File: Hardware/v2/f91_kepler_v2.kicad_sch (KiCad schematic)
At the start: 89 parts, among them J1 LS013B7DH03 FPC, Q1 FS8205A, SW1 BTN1/BSL, SW2 BTN2, SW3 BTN3, U1 CC2652R7RGZ, U2 BQ51050B, U3 DW01A, U4 XC6206P302MR, U5 LIS2DW12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

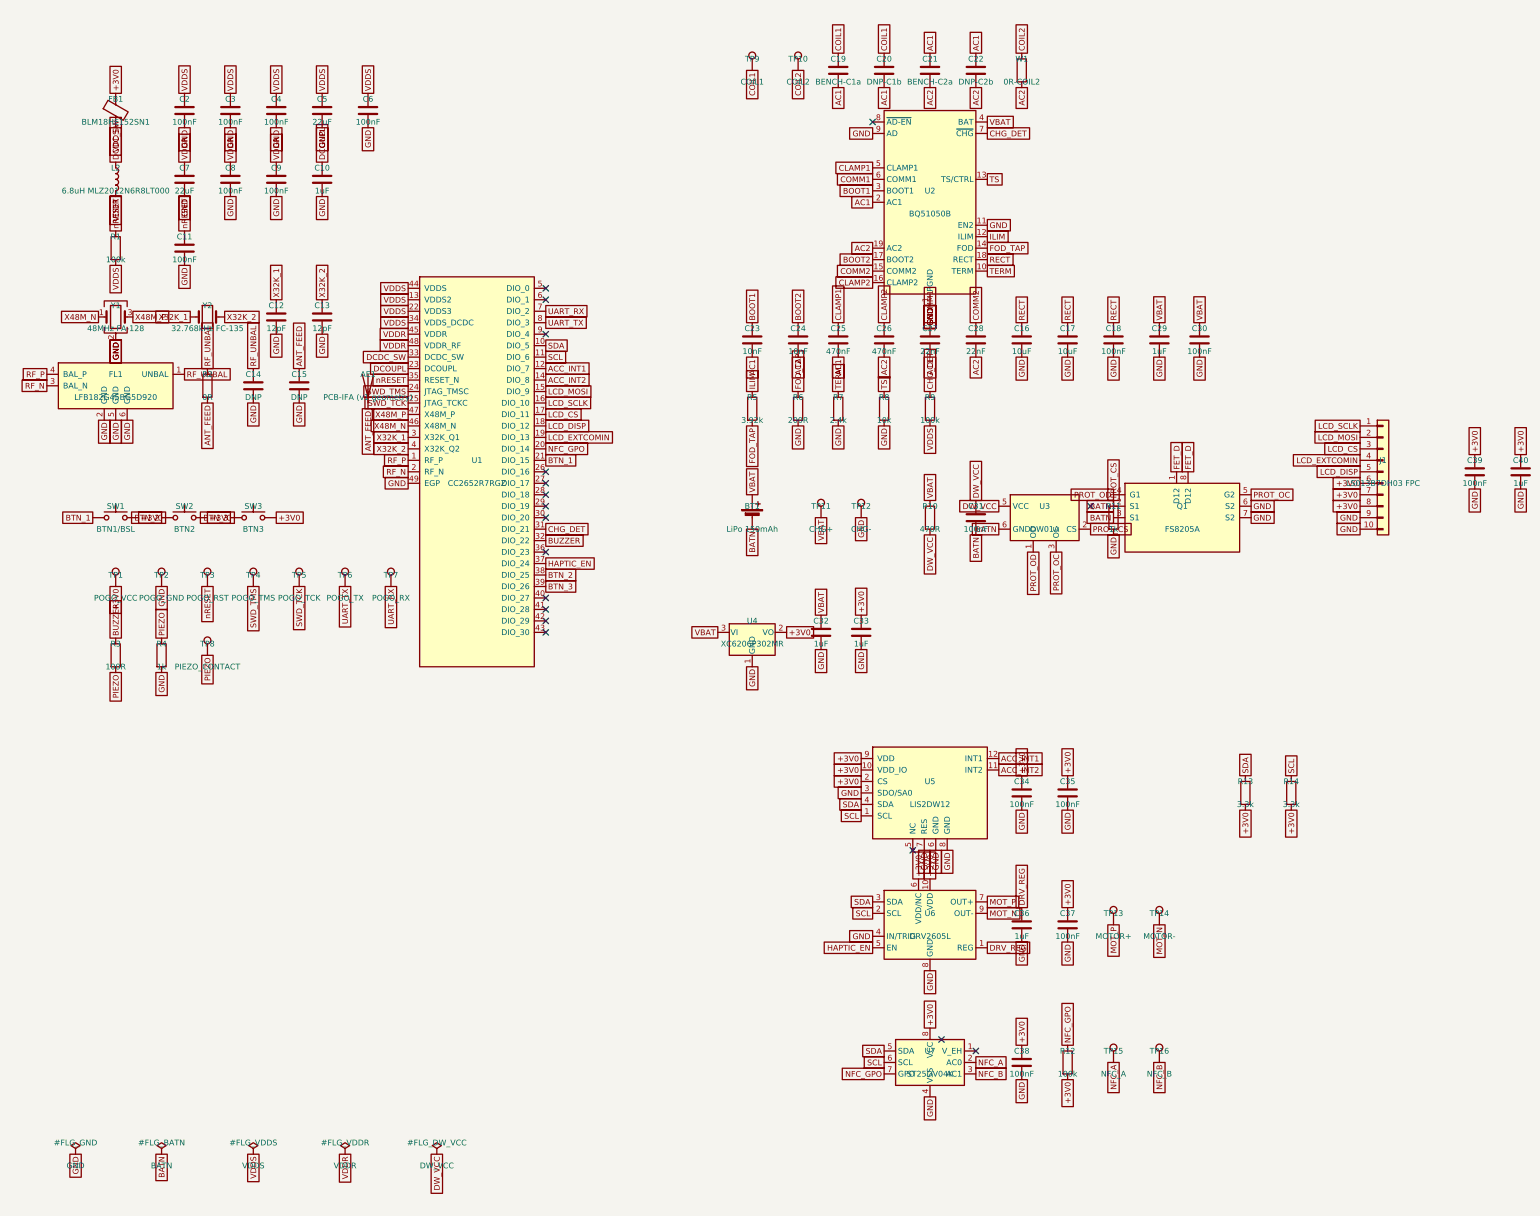
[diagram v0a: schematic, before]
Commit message: fix(hw/v2): sync AE1 schematic symbol to chip antenna
Update AE1 in the schematic to match the PCB chip-antenna swap:
- Value: "PCB-IFA (v1 geometry)" -> "2450AT18A100"
- Footprint: f91_footprints:ANT_v1_IFA -> f91_footprints:ANT_2450AT18A100

Device:Antenna symbol kept (pin1 = Feed = ANT_FEED, matches board pad1);
footprint pad2 (NC) is an unmapped mechanical pad, which KiCad allows.
schematic-parity: AE1 has no net conflict. The remaining parity items
(105 blank-lib-nickname footprint mismatches, 17 unconnected-GPIO net
entries, 1 stray pin) are pre-existing project-wide noise, not from this
change.
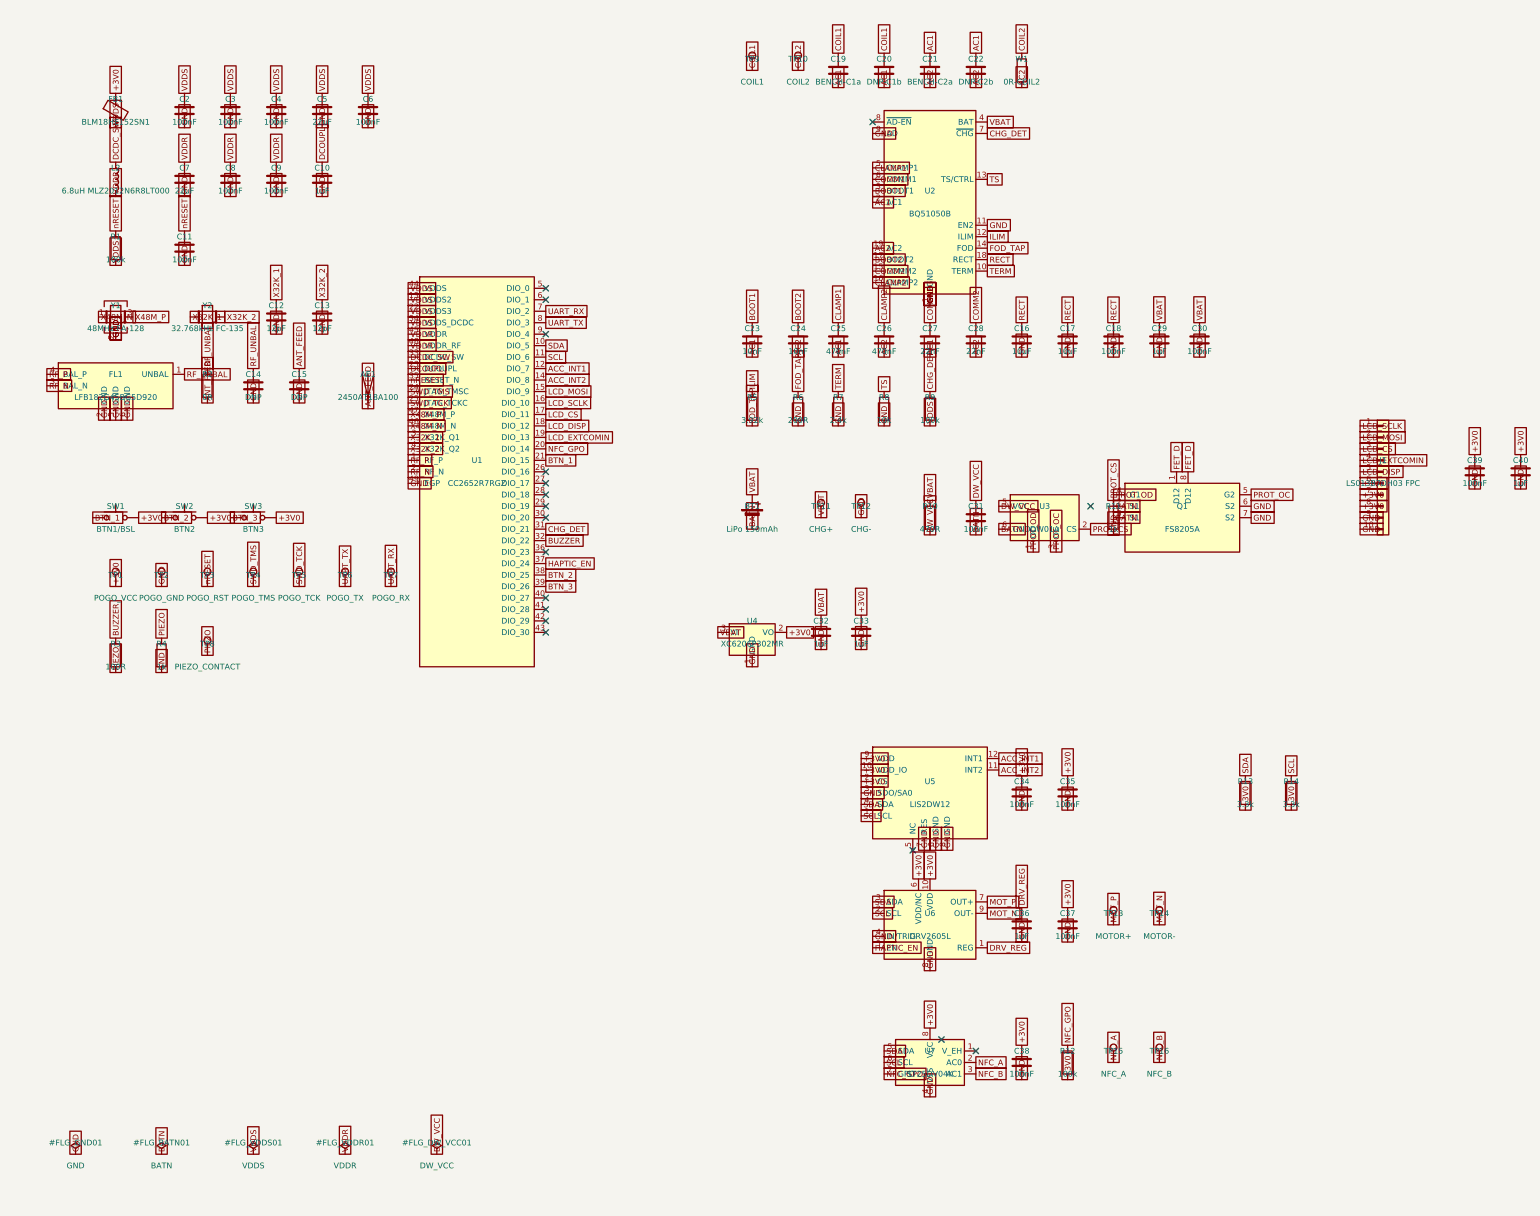
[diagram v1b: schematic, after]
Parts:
- AE1: value PCB-IFA (v1 geometry) -> 2450AT18A100; footprint f91_footprints:ANT_v1_IFA -> f91_footprints:ANT_2450AT18A100

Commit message: fix(hw/v2): close PCB<->schematic parity debt (123 -> 1)
Board was generated with blank footprint library nicknames and a few
metadata gaps, producing 123 schematic-parity mismatches that would fight
"update PCB from schematic". Closed almost all:

- fix_fpids.py: set each board footprint FPID nickname from the schematic
  (item names already matched -> no geometry change). Clears 105 name
  mismatches.
- fix_tp_bom.py: TP1-16 symbols in_bom/in_pos_files yes -> no. Test points
  (pogo pads + taps) are not orderable BOM parts; the footprints already
  excluded them. Clears 16 attribute mismatches.
- fix_unconnected_nets.py: assign the schematic's single-pad
  "unconnected-(...)" nets (spare U1/U2/U3/U5/U7 pins) to the matching
  netless board pads. Clears 17 net_conflicts.

Remaining (all benign, documented):
- parity 1: U7 ST25DV symbol pin 9 = "NC" (hidden); SO8 footprint correctly
  has no pad 9. KiCad flags NC pins without pads as warnings.
- ERC 2: U4 lib_symbol_mismatch (stale embedded copy vs Regulator_Linear;
  fix via Eeschema "Update Symbols from Library"); U5 pin_to_pin (SDO/SA0
  tied to GND for I2C address select — intentional, ERC false positive).

DRC fab-blocking still 0. Schematic migrated f91gen -> eeschema format.
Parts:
- TP1, TP10, TP11, TP12, TP13, TP14, TP15, TP16, TP2, TP3, TP4, TP5, TP6, TP7, TP8, TP9: now left out of the parts list
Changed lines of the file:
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@@
 		(body_style 1)
 		(exclude_from_sim no)
-		(in_bom yes)
+		(in_bom no)
 		(on_board yes)
-		(in_pos_files yes)
+		(in_pos_files no)
 		(dnp no)
 		(property "Reference" "TP3"
@@
 		(body_style 1)
 		(exclude_from_sim no)
-		(in_bom yes)
+		(in_bom no)
 		(on_board yes)
-		(in_pos_files yes)
+		(in_pos_files no)
 		(dnp no)
 		(property "Reference" "TP7"
@@
 		(body_style 1)
 		(exclude_from_sim no)
-		(in_bom yes)
+		(in_bom no)
 		(on_board yes)
-		(in_pos_files yes)
+		(in_pos_files no)
 		(dnp no)
 		(property "Reference" "TP13"
@@
 		(body_style 1)
 		(exclude_from_sim no)
-		(in_bom yes)
+		(in_bom no)
 		(on_board yes)
-		(in_pos_files yes)
+		(in_pos_files no)
 		(dnp no)
 		(property "Reference" "TP14"
@@
 		(body_style 1)
 		(exclude_from_sim no)
-		(in_bom yes)
+		(in_bom no)
 		(on_board yes)
-		(in_pos_files yes)
+		(in_pos_files no)
 		(dnp no)
 		(property "Reference" "TP10"
@@
 		(body_style 1)
 		(exclude_from_sim no)
-		(in_bom yes)
+		(in_bom no)
 		(on_board yes)
-		(in_pos_files yes)
+		(in_pos_files no)
 		(dnp no)
 		(property "Reference" "TP5"
@@
 		(body_style 1)
 		(exclude_from_sim no)
-		(in_bom yes)
+		(in_bom no)
 		(on_board yes)
-		(in_pos_files yes)
+		(in_pos_files no)
 		(dnp no)
 		(property "Reference" "TP1"
@@
 		(body_style 1)
 		(exclude_from_sim no)
-		(in_bom yes)
+		(in_bom no)
 		(on_board yes)
-		(in_pos_files yes)
+		(in_pos_files no)
 		(dnp no)
 		(property "Reference" "TP11"
@@
 		(body_style 1)
 		(exclude_from_sim no)
-		(in_bom yes)
+		(in_bom no)
 		(on_board yes)
-		(in_pos_files yes)
+		(in_pos_files no)
 		(dnp no)
 		(property "Reference" "TP9"
@@
 		(body_style 1)
 		(exclude_from_sim no)
-		(in_bom yes)
+		(in_bom no)
 		(on_board yes)
-		(in_pos_files yes)
+		(in_pos_files no)
 		(dnp no)
 		(property "Reference" "TP2"
@@
 		(body_style 1)
 		(exclude_from_sim no)
-		(in_bom yes)
+		(in_bom no)
 		(on_board yes)
-		(in_pos_files yes)
+		(in_pos_files no)
 		(dnp no)
 		(property "Reference" "TP16"
@@
 		(body_style 1)
 		(exclude_from_sim no)
-		(in_bom yes)
+		(in_bom no)
 		(on_board yes)
-		(in_pos_files yes)
+		(in_pos_files no)
 		(dnp no)
 		(property "Reference" "TP4"
@@
 		(body_style 1)
 		(exclude_from_sim no)
-		(in_bom yes)
+		(in_bom no)
 		(on_board yes)
-		(in_pos_files yes)
+		(in_pos_files no)
 		(dnp no)
 		(property "Reference" "TP15"
@@
 		(body_style 1)
 		(exclude_from_sim no)
-		(in_bom yes)
+		(in_bom no)
 		(on_board yes)
-		(in_pos_files yes)
+		(in_pos_files no)
 		(dnp no)
 		(property "Reference" "TP12"
@@
 		(body_style 1)
 		(exclude_from_sim no)
-		(in_bom yes)
+		(in_bom no)
 		(on_board yes)
-		(in_pos_files yes)
+		(in_pos_files no)
 		(dnp no)
 		(property "Reference" "TP6"
@@
 		(body_style 1)
 		(exclude_from_sim no)
-		(in_bom yes)
+		(in_bom no)
 		(on_board yes)
-		(in_pos_files yes)
+		(in_pos_files no)
 		(dnp no)
 		(property "Reference" "TP8"
